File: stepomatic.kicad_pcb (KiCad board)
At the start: 2 copper layers, 50 x 30 mm, 80 parts, among them J1 I2C, J2 Conn_01x03, J4 USB_B_Micro, Q1 MMBT3904, Q2 MMBT3904, SW1 Mode, SW2 RST, U1 HDC1080DMBR, U3 ULN2003A, U4 CH340C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

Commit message: Minor changes on PCB
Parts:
- moved G*** 0.73 mm to (115.6, 87.4)
- moved G*** 0.22 mm to (107.9, 97.4)
- moved C8 0.08 mm to (108.3, 86.8)
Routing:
- net GND: track 48.8 -> 47.8 mm, vias 18 -> 17
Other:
- board text added: "v1.0 26.02.24"
- board text removed: "v1.0 25.02.24"

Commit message: Finish up PCB backside artwork
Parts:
- added G***: LOGO, LOGO, B.Cu at (110.3, 72.8)
- added G***: LOGO, LOGO, B.Cu at (116.7, 80.2)
- added G***: LOGO, LOGO, B.Cu at (113.1, 77.8)
- J2: value Conn_01x03 -> 5V Switch
- moved G*** 1.89 mm to (109.8, 72.2)
- moved G*** 1.33 mm to (112.9, 81.8)
- moved TP1 0.11 mm to (122.7, 97.0)
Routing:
- net NEOPIXEL: track 29.0 -> 31.5 mm
- net RX: track 30.4 -> 32.6 mm
- net IR: track 22.2 -> 23.5 mm
- net RESET: track 60.8 -> 62.2 mm
- net GND: track 47.8 -> 48.7 mm
- net I2C_SCL: track 30.2 -> 30.7 mm

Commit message: Add artists signature
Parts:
- added G***: LOGO, LOGO, B.Cu at (101.3, 96.0)
- added G***: LOGO, LOGO, F.Cu at (135.6, -0.51)
- moved G*** 0.92 mm to (102.6, 98.6)

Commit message: Add commit label
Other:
- board text added: "Commit:"
- board text added: "v1.0 28.02.24"
- board text removed: "v1.0 26.02.24"
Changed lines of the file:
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@@
   (gr_arc (start 146 70) (mid 148.828427 71.171573) (end 150 74)
     (stroke (width 0.1) (type solid)) (layer "Edge.Cuts"))
-  (gr_text "v1.0\n26.02.24" (at 148.282479 92.73096 90) (layer "F.SilkS")
+  (gr_text "v1.0\n28.02.24" (at 148.282479 92.73096 90) (layer "F.SilkS")
     (effects (font (size 1 1) (thickness 0.1)))
   )
+  (gr_text "Commit: " (at 130.060288 99.378202) (layer "F.SilkS")
+    (effects (font (size 0.75 0.75) (thickness 0.1)) (justify left))
+  )
   (gr_text "besi/\nstepomatic" (at 107.945798 96.368563 90) (layer "F.SilkS")

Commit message: Clean up silkscreen
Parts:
- removed the G*** at (135.6, -0.51)
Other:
- board text added: "Commit: 98cb2e"
- board text removed: "Commit:"

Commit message: Release candidate v1.0
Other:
- board text added: "Commit: 70c2a7"
- board text removed: "Commit: 98cb2e"
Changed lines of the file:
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@@
     (effects (font (size 1 1) (thickness 0.1)))
   )
-  (gr_text "Commit: 98cb2e" (at 130.060288 99.378202) (layer "F.SilkS")
+  (gr_text "Commit: 70c2a7" (at 130.060288 99.378202) (layer "F.SilkS")
     (effects (font (size 0.75 0.75) (thickness 0.1)) (justify left))
   )

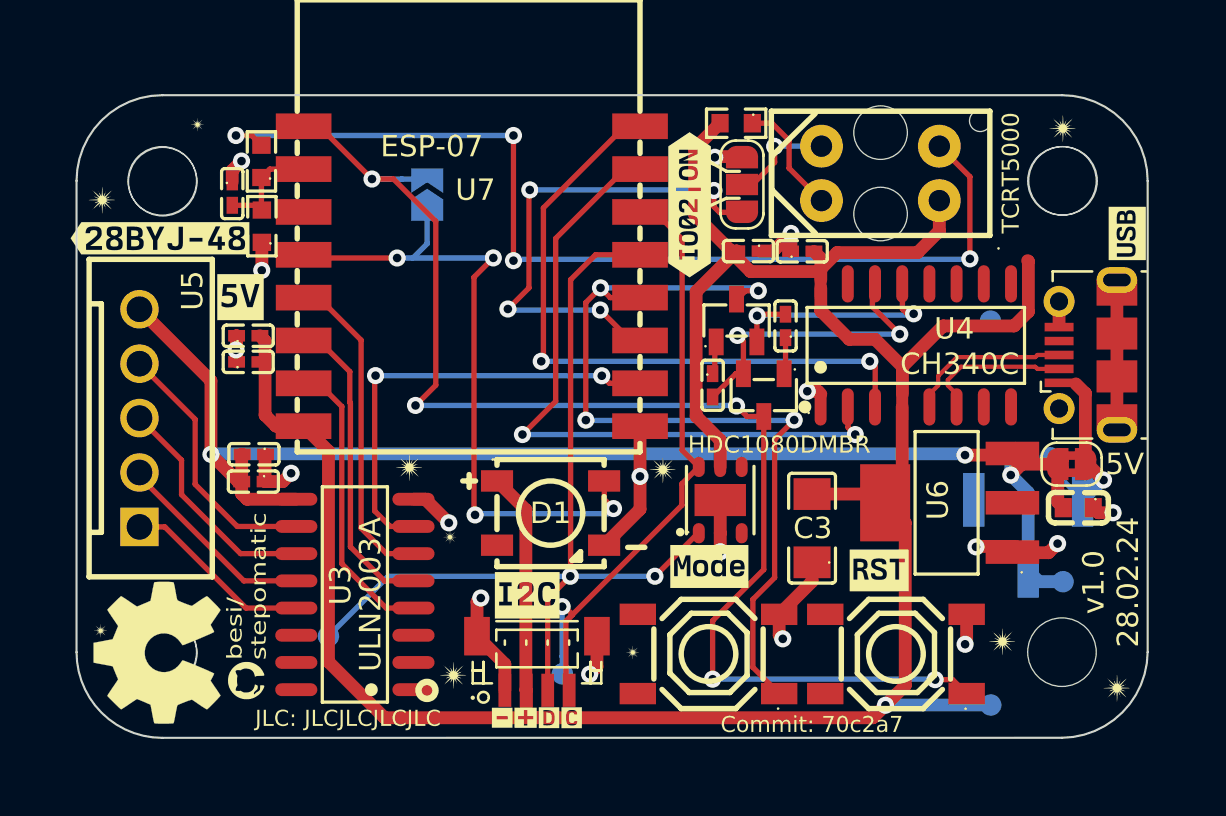
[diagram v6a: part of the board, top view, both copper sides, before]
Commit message: Change resistors on TCRT5000 to 20k and 10k
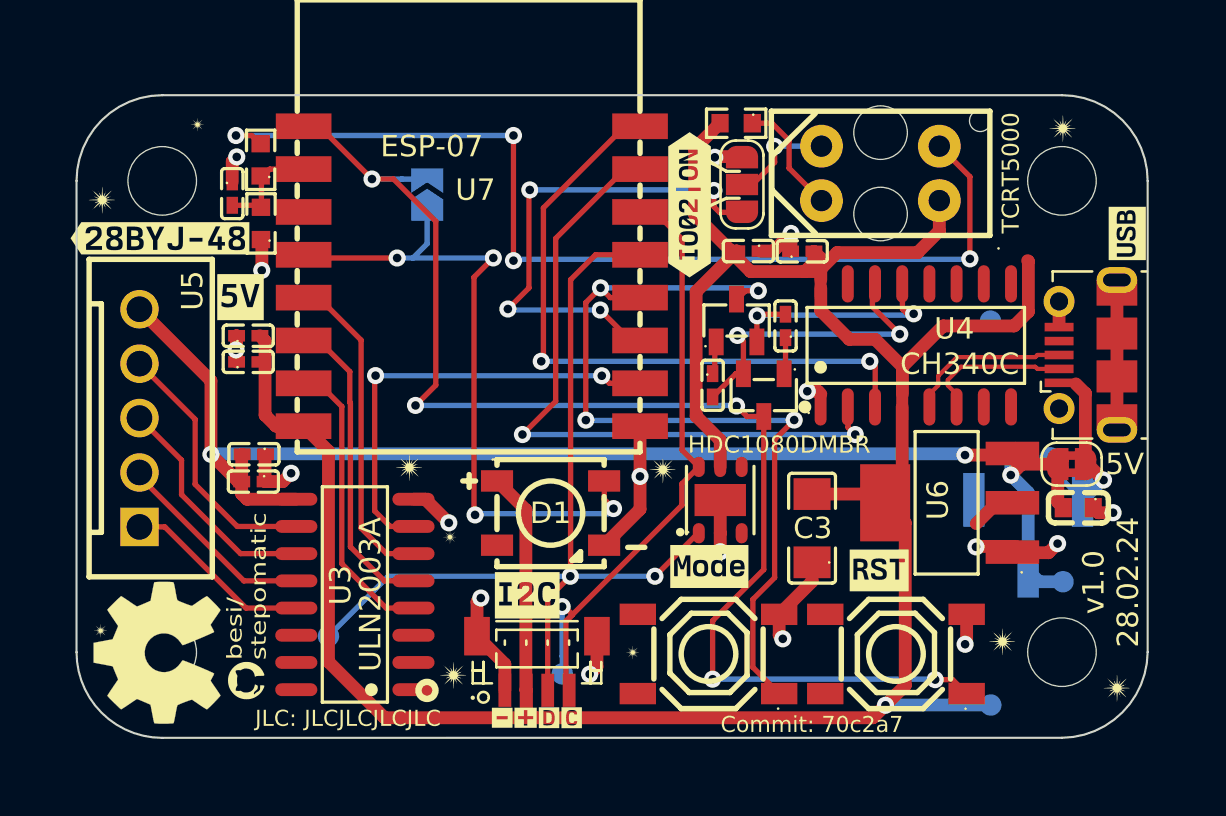
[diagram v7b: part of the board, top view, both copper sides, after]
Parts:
- removed H3: MountingHole, MountingHole:MountingHole_3.2mm_M3
- added Hee: MountingHole, MountingHole:MountingHole_3.2mm_M3, F.Cu at (146.0, 74.0)
- R3: value 200k -> 20k
- R5: value 100k -> 10k
- moved H2 42.0 mm to (146.0, 96.0)
- moved H4 42.0 mm to (104.0, 96.0)
- moved R5 0.14 mm to (108.6, 76.0)
- moved R3 0.08 mm to (108.6, 73.0)
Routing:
- net +3V3: track 129.3 -> 132.6 mm

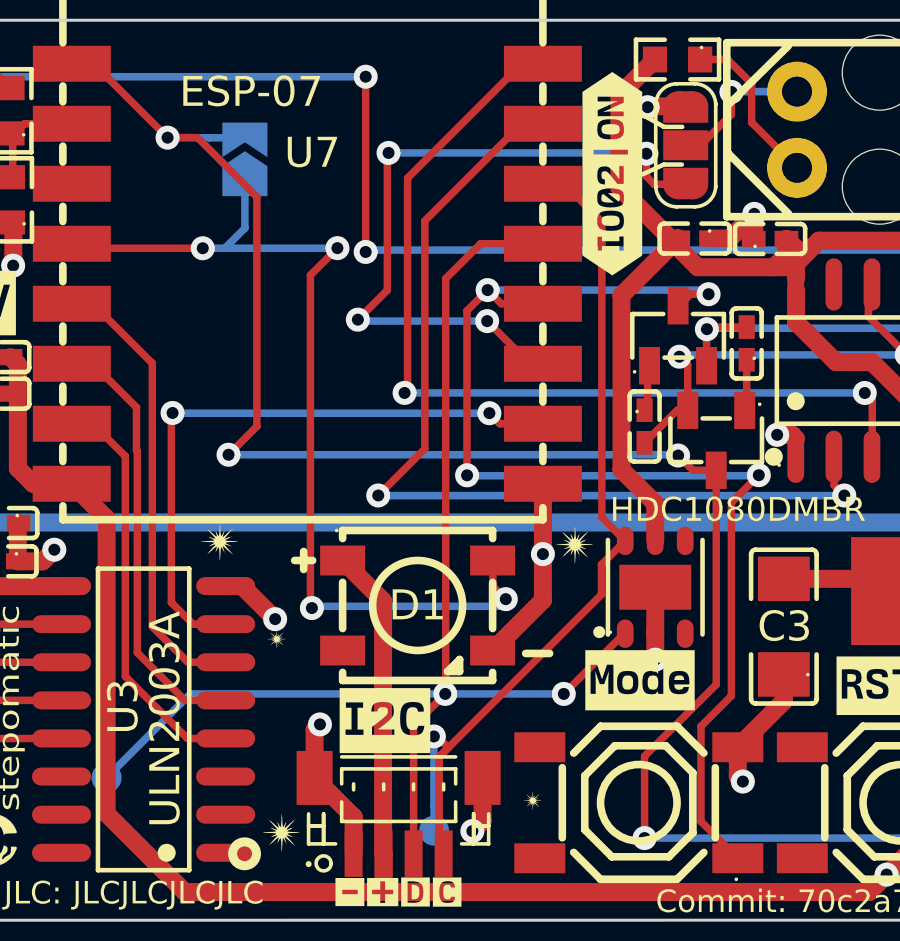
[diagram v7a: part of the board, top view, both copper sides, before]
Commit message: Add neopixel testpads
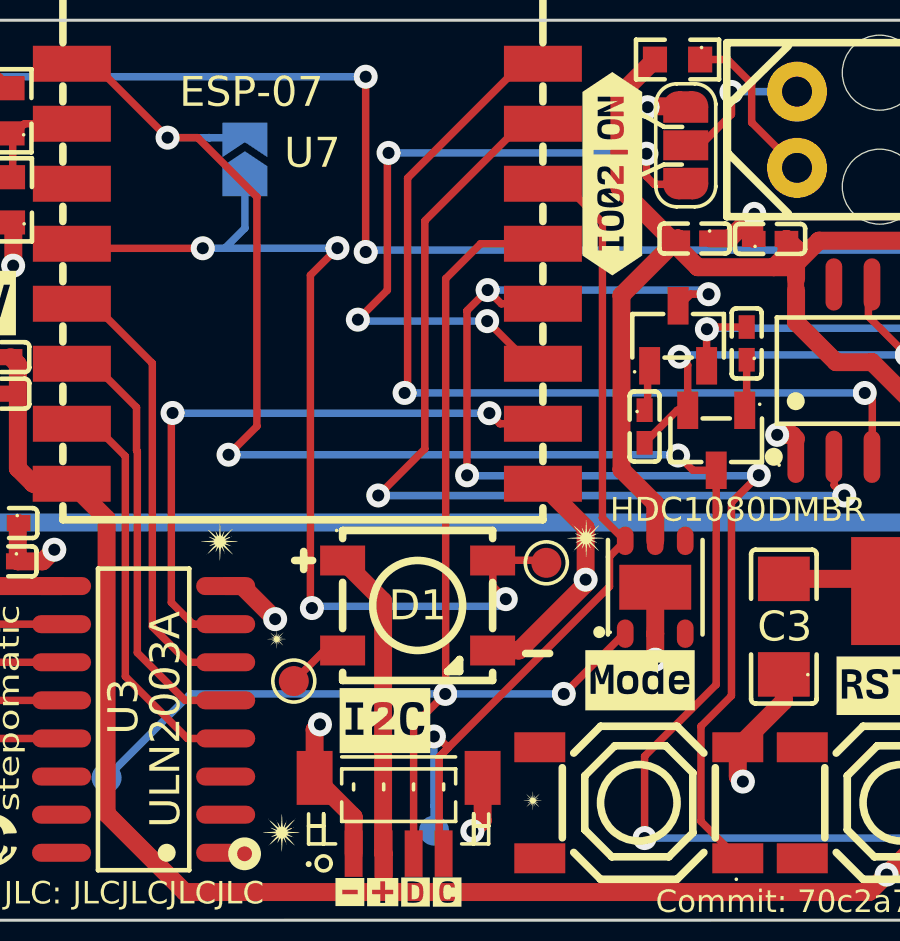
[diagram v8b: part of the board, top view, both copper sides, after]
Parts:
- added TP7: NP_OUT, TestPoint:TestPoint_Pad_D1.0mm, F.Cu at (118.0, 92.0)
- added TP8: NP_IN, TestPoint:TestPoint_Pad_D1.0mm, F.Cu at (126.4, 88.1)
- moved G*** 0.43 mm to (127.8, 87.3)
- renumbered Hee to H3
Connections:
- D1 pad 2: unconnected-(D1-DOUT-Pad2) -> NEOPIXEL_OUT
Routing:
- net NEOPIXEL_OUT: track 0.00 -> 2.05 mm
- net NEOPIXEL: track 31.5 -> 33.3 mm
- net GND: track 48.8 -> 50.5 mm
